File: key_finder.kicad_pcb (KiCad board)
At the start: 2 copper layers, 20 x 14 mm, 18 parts, among them U1 NRF52832, X1 32MHz, X2 32.768kHz

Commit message: end of shematic
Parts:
- added BT1: Battery, Battery:BatteryHolder_Keystone_103_1x20mm, F.Cu at (137.0, 137.2)
- added BZ1: Buzzer, Buzzer_Beeper:Buzzer_CUI_CPT-9019S-SMT, F.Cu at (128.1, 104.1)
- added D1: LED, LED_SMD:LED_0805_2012Metric, F.Cu at (141.3, 114.3)
- added R1: 330, Resistor_SMD:R_0805_2012Metric, F.Cu at (136.2, 114.3)
- added R2: 10k, Resistor_SMD:R_0805_2012Metric, F.Cu at (136.2, 109.2)
- added R3: 10k, Resistor_SMD:R_0805_2012Metric, F.Cu at (151.5, 119.4)
- added SW1: SW_Push, Button_Switch_THT:SW_PUSH_6mm_H7.3mm, F.Cu at (132.1, 121.3)
- added SW2: SW_Push, Button_Switch_SMD:SW_Push_1P1T_NO_CK_KMR2, F.Cu at (160.5, 113.5)
- U1: footprint QFN40P600X600X90-48_N -> Package_DFN_QFN:QFN-48-1EP_6x6mm_P0.4mm_EP4.2x4.2mm
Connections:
- net P0.02 renamed /P0.02
- net P0.03 renamed /P0.03
- net P0.05 renamed /P0.05
- net P0.07 renamed /P0.07
- net P0.08 renamed /P0.08
- net P0.09 renamed /P0.09
- net P0.11 renamed /P0.11
- net P0.12 renamed /P0.12
- net P0.13 renamed /P0.13
- net P0.14 renamed /P0.14
- net P0.15 renamed /P0.15
- net P0.16 renamed /P0.16
- net P0.17 renamed /P0.17
- net P0.18/SWO renamed /P0.18/SWO
- net P0.19 renamed /P0.19
- net P0.20 renamed /P0.20
- net P0.22 renamed /P0.22
- net P0.23 renamed /P0.23
- net P0.24 renamed /P0.24
- net P0.25 renamed /P0.25
- net P0.26 renamed /P0.26
- net P0.27 renamed /P0.27
- net P0.28 renamed /P0.28
- net P0.29 renamed /P0.29
- net P0.30 renamed /P0.30
- net P0.31 renamed /P0.31
- net SWDCLK renamed /SWDCLK
- net SWDIO renamed /SWDIO
- U1 pad 1: DEC1 -> /DEC1
- U1 pad 12: P0.10 -> /P0.10
- U1 pad 13: VDD_P3V3 -> VCC
- U1 pad 2: P0.00/XL1 -> /P0.00/XL1
- U1 pad 24: P0.21/RESET -> /P0.21/RESET
- U1 pad 3: P0.01/XL2 -> /P0.01/XL2
- U1 pad 30: ANT -> Net-(U1-ANT@30)
- U1 pad 32: DEC2 -> /DEC2
- U1 pad 33: DEC3 -> /DEC3
- U1 pad 34: X1 -> Net-(U1-XC1@34)
- U1 pad 35: N$3 -> Net-(U1-XC2@35)
- U1 pad 36: VDD_P3V3 -> VCC
- U1 pad 44: (no net) -> unconnected-(U1-N.C.@44-Pad44)
- U1 pad 46: DEC4 -> /DEC4
- U1 pad 47: N$4 -> Net-(U1-DCC@47)
- U1 pad 48: VDD_P3V3 -> VCC
- U1 pad 6: P0.04 -> /P0.04
- U1 pad 8: P0.06 -> /P0.06
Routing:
- net P0.10: track 7.50 -> 0.00 mm
- net P0.06: track 7.50 -> 0.00 mm
- net P0.04: track 7.50 -> 0.00 mm
- net /P0.10: track 0.00 -> 7.50 mm
- net /P0.06: track 0.00 -> 7.50 mm
- net /P0.04: track 0.00 -> 7.50 mm
- net P0.21/RESET: track 2.50 -> 0.00 mm
- net /P0.21/RESET: track 0.00 -> 2.50 mm
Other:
- board size 20 x 14 mm -> 45.7 x 55.9 mm

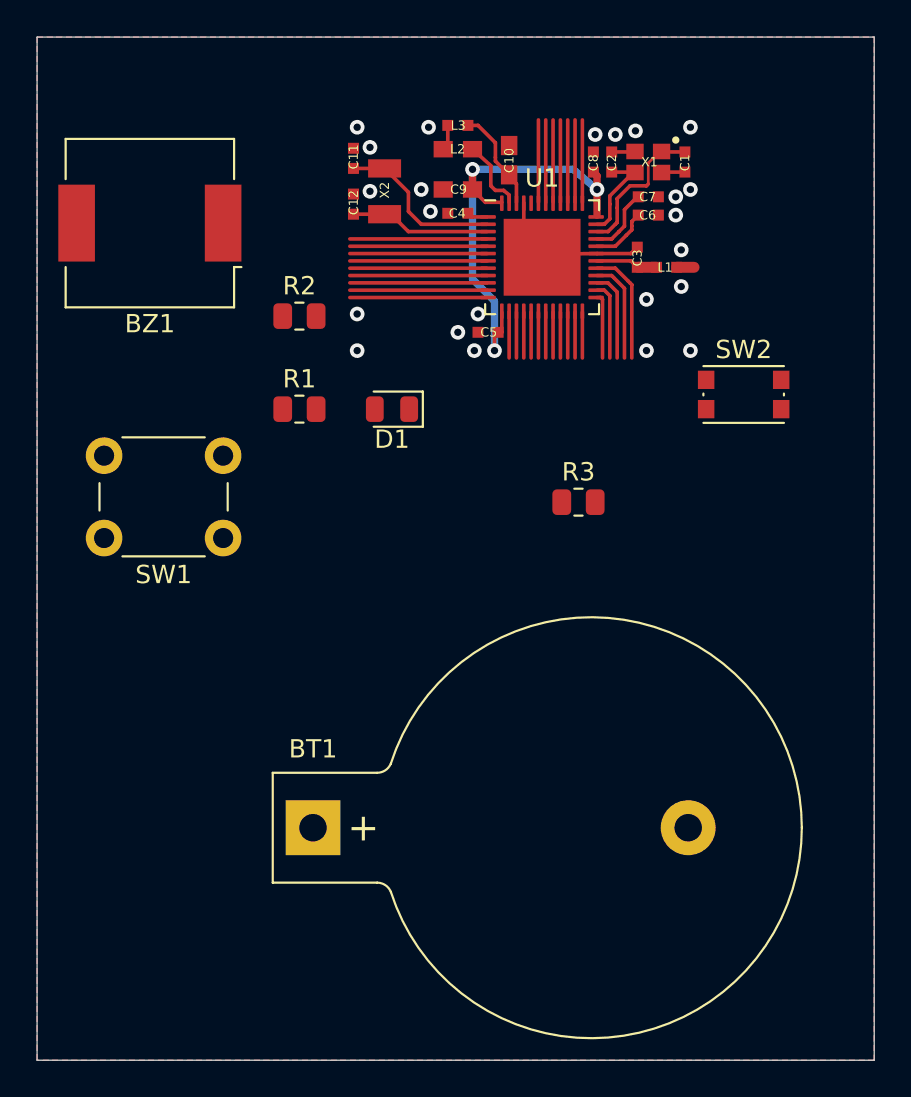
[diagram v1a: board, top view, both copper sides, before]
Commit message: change battery + relier les composants
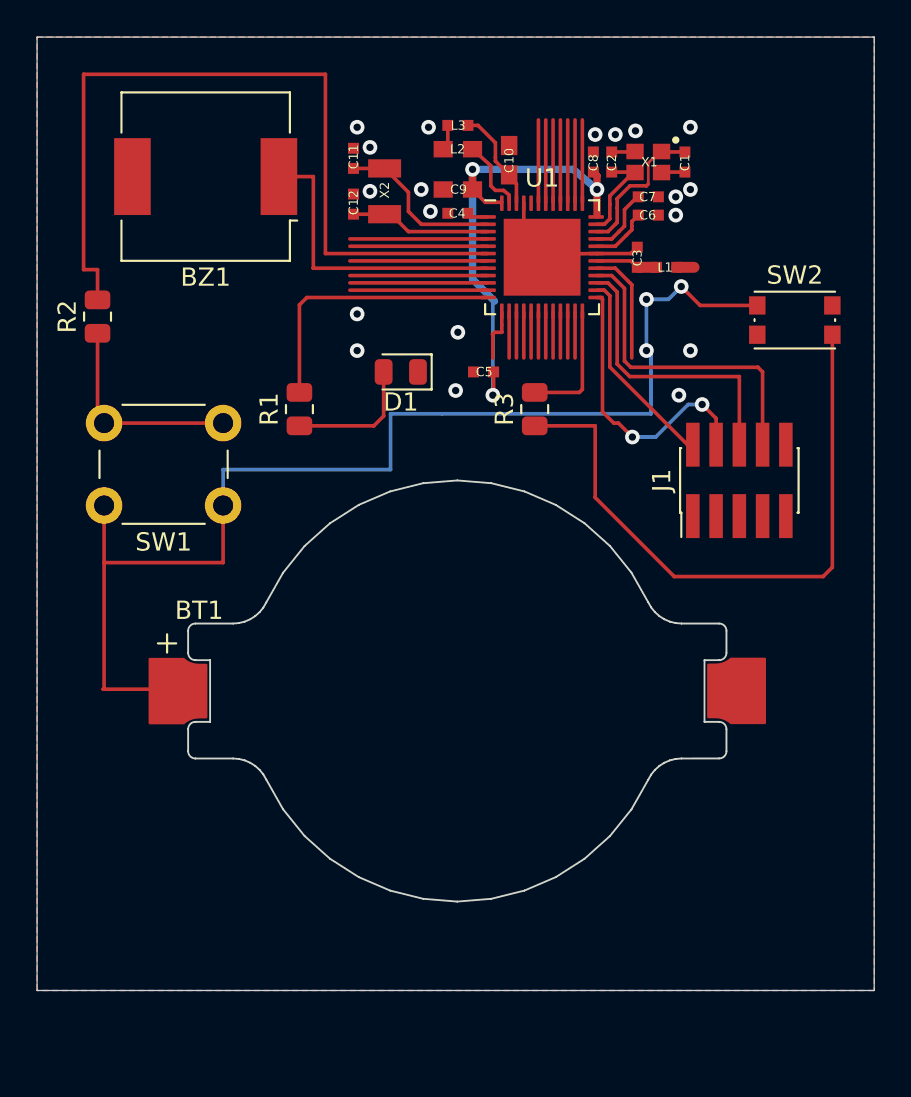
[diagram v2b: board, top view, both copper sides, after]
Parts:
- added J1: Conn_ARM_JTAG_SWD_10, Connector_PinHeader_1.27mm:PinHeader_2x05_P1.27mm_Vertical_SMD, F.Cu at (160.3, 118.2)
- BT1: footprint Battery:BatteryHolder_Keystone_103_1x20mm -> Battery:BatteryHolder_Keystone_1057_1x2032
- moved R2 11.0 mm to (125.2, 109.2), turned to 90 degrees
- moved BT1 10.9 mm to (144.9, 129.7)
- moved R3 5.61 mm to (149.1, 114.3), turned to 90 degrees
- moved SW2 4.93 mm to (163.3, 109.4)
- moved BZ1 3.97 mm to (131.1, 101.6)
- moved C5 2.18 mm to (146.3, 112.3)
- moved D1 2.09 mm to (141.8, 112.3)
- moved SW1 1.78 mm to (132.1, 119.6)
- turned R1 to 90 degrees
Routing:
- net VCC: track 0.00 -> 68.3 mm, vias 0 -> 3
- net /P0.04: track 7.50 -> 44.9 mm
- net Net-(R3-Pad1): track 0.00 -> 34.9 mm
- net /SWDCLK: track 3.54 -> 15.7 mm, vias 0 -> 2
- net /P0.23: track 5.59 -> 17.5 mm
- net Net-(R2-Pad1): track 0.00 -> 11.6 mm
- net /P0.22: track 4.91 -> 15.9 mm
- net /P0.06: track 7.50 -> 16.4 mm
- net /P0.10: track 7.50 -> 15.2 mm
- net Net-(D1-A): track 0.00 -> 7.23 mm
- net /SWDIO: track 4.22 -> 11.0 mm
- net /P0.21/RESET: track 2.50 -> 6.89 mm
- net VDD_P3V3: track 25.6 -> 26.9 mm
- net GND: vias 23 -> 19
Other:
- board size 45.7 x 55.9 mm -> 45.7 x 52.1 mm

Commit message: sceance 2
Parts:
- added MK1: Microphone, Sensor_Audio:CUI_CMC-4013-SMT, B.Cu at (179.2, 95.0)
- BT1: footprint Battery:BatteryHolder_Keystone_1057_1x2032 -> Battery:BatteryHolder_Keystone_1060_1x2032; moved to B.Cu
- SW1: footprint Button_Switch_THT:SW_PUSH_6mm_H7.3mm -> Button_Switch_SMD:SW_Push_1P1T_NO_CK_KMR2
- moved SW1 69.6 mm to (192.5, 85.1)
- moved BT1 64.9 mm to (192.0, 85.1), turned to 180 degrees
- moved BZ1 60.8 mm to (186.8, 77.0), turned to 0 degrees
- moved R2 56.9 mm to (173.7, 79.5), turned to 180 degrees
- moved R3 56.9 mm to (194.7, 80.3), turned to 180 degrees
- moved C6 54.4 mm to (202.9, 77.4)
- moved C7 54.4 mm to (202.9, 76.4)
- moved C3 52.5 mm to (200.3, 80.0)
- moved L1 52.5 mm to (201.9, 80.6)
- moved C1 50.8 mm to (201.2, 75.2)
- moved C2 50.8 mm to (197.2, 75.2)
- moved C8 50.8 mm to (196.2, 75.2)
- moved X1 50.8 mm to (199.2, 75.2)
- moved J1 47.4 mm to (199.6, 91.9)
- moved SW2 45.5 mm to (200.9, 83.8)
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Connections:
- net /P0.00/XL1 renamed Net-(U1-P0.00/XL1@02)
- net /P0.01/XL2 renamed Net-(U1-P0.01/XL2@03)
- C1 pad 1: X1 -> Net-(U1-XC1@34)
- C2 pad 1: N$3 -> Net-(U1-XC2@35)
- C3 pad 1: ANT -> Net-(U1-ANT@30)
- C5 pad 1: VDD_P3V3 -> VCC
- C6 pad 1: DEC2 -> /DEC2
- C7 pad 1: DEC3 -> /DEC3
- C8 pad 1: VDD_P3V3 -> VCC
- C9 pad 1: VDD_P3V3 -> VCC
- L1 pad 1: ANT -> Net-(U1-ANT@30)
- R1 pad 2: /P0.10 -> /P0.09
- X1 pad 1: X1 -> Net-(U1-XC1@34)
- X1 pad 3: N$3 -> Net-(U1-XC2@35)
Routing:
- net VCC: track 68.3 -> 132.5 mm, vias 3 -> 8
- net /P0.21/RESET: track 6.89 -> 63.8 mm, vias 0 -> 2
- net VDD_P3V3: track 26.9 -> 0.00 mm, vias 3 -> 0
- net Net-(U1-XC1@34): track 0.00 -> 26.2 mm, vias 0 -> 2
- net Net-(U1-XC2@35): track 0.00 -> 25.7 mm, vias 0 -> 2
- net Net-(R3-Pad1): track 34.9 -> 9.80 mm
- net RF: track 0.95 -> 25.1 mm, vias 0 -> 1
- net /DEC3: track 0.00 -> 21.2 mm, vias 0 -> 2
- net /DEC2: track 0.00 -> 20.9 mm, vias 0 -> 2
- net Net-(U1-ANT@30): track 0.00 -> 19.6 mm, vias 0 -> 2
- net /P0.04: track 44.9 -> 26.0 mm, vias 0 -> 2
- net /P0.06: track 16.4 -> 31.4 mm, vias 0 -> 2
- net GND: track 27.1 -> 15.2 mm, vias 19 -> 12
- net Net-(R2-Pad1): track 11.6 -> 21.5 mm
- net /P0.10: track 15.2 -> 5.42 mm, vias 0 -> 1
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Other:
- board size 45.7 x 52.1 mm -> 39 x 31 mm

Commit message: correct some details
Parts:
- C3, L1: moved to B.Cu
- moved C3 2.27 mm to (201.7, 81.9), turned to 0 degrees
- moved L1 0.85 mm to (201.2, 80.3), turned to 90 degrees
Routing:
- net RF: track 25.1 -> 21.3 mm, vias 1 -> 0
- net Net-(U1-ANT@30): track 19.6 -> 18.2 mm, vias 2 -> 1
